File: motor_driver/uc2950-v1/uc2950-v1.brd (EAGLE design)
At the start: 165.6 x 63.7 mm, 76 parts, among them IC1 ATMEGA2560-16AU, IC2 ATMEGA2560-16AU, IC3 ATMEGA2560-16AU, IC4 ACS712, IC5 ACS712, IC6 ACS712, Y2 16MHz, Y3 16MHz, Y4 16MHz

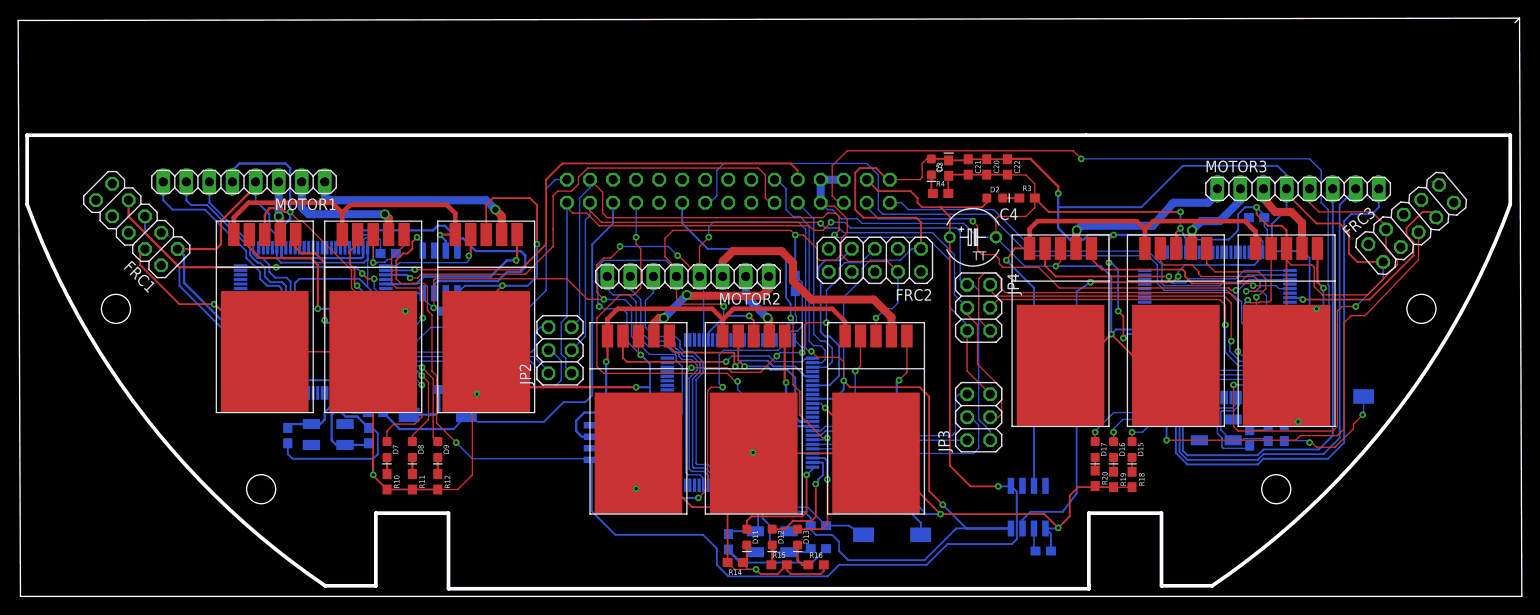
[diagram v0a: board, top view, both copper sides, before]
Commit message: added 12v, fixed previous issues
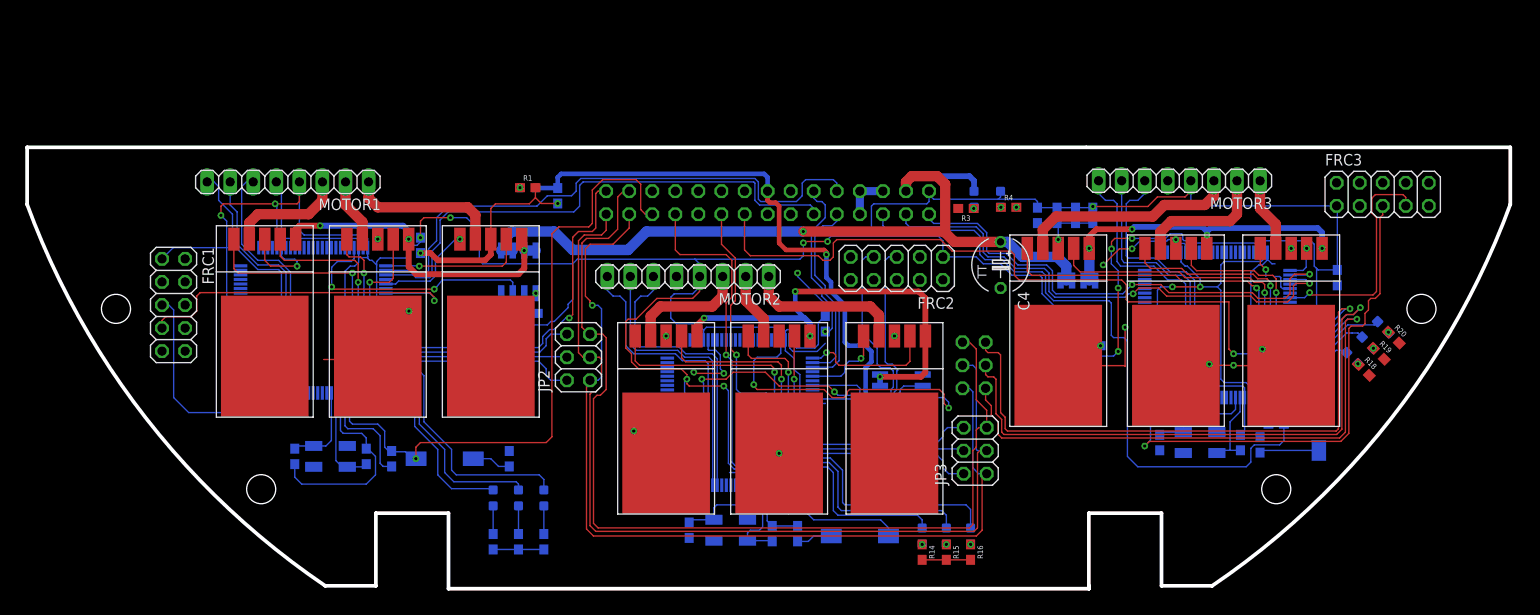
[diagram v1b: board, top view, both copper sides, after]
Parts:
- added C1: 10uF, SparkFun-Capacitors:0603-POLAR
- added D1: Yellow, SparkFun-LED:LED-0603
- added R1: 1k, SparkFun-Resistors:0603
- moved R20 36.4 mm to (150.7, 28.8), turned to 315 degrees
- moved D17 34.5 mm to (149.6, 30.0), flipped to the bottom, turned to 225 degrees
- moved R19 32.3 mm to (149.1, 27.1), turned to 315 degrees
- moved IC5 32.2 mm to (96.5, 22.9)
- moved C23 31.3 mm to (96.4, 19.1)
- moved D16 30.4 mm to (147.9, 28.3), flipped to the bottom, turned to 225 degrees
- moved R18 28.2 mm to (147.4, 25.3), turned to 315 degrees
- moved MIC6 28.2 mm to (90.4, 25.4)
- moved D15 26.3 mm to (146.2, 26.6), flipped to the bottom, turned to 225 degrees
- moved MIC7 25.4 mm to (134.1, 35.1)
- moved MIC9 25.1 mm to (108.5, 35.1)
- moved C24 23.3 mm to (117.6, 27.9)
- moved IC6 23.3 mm to (116.0, 32.8)
- moved MIC4 23.1 mm to (65.3, 25.4)
- moved R14 20.6 mm to (98.8, 5.21), turned to 270 degrees
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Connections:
- removed net N$11: C2.1, IC1.98
- removed net N$24: C3.1, IC3.98
- removed net N$26: C14.1, IC2.98
- new net 12V: C1.+, D1.A, IC5.1, IC5.2, JP1.16
- new net N$1: D1.C, R1.1
- net 18V: now also IC4.2, IC6.2; no longer IC5.1
- net 5V: now also C14.1, C2.1, C3.1, IC1.98, IC2.98, IC3.98
- net ACS1: now also IC4.4, MIC1.P$5, MIC2.P$5, MIC3.P$5; no longer MIC1.P$1, MIC2.P$1, MIC3.P$1
- net ACS2: now also IC5.4, MIC4.P$5, MIC5.P$5, MIC6.P$5; no longer MIC4.P$1, MIC5.P$1, MIC6.P$1
- net ACS3: now also IC6.4, MIC7.P$5, MIC8.P$5, MIC9.P$5; no longer MIC7.P$1, MIC8.P$1, MIC9.P$1
- net GND: now also C1.-, R1.2
- net M11: now also MIC3.P$2; no longer MIC3.P$4
- net M12: now also MIC6.P$2; no longer MIC6.P$4
- net M13: now also MIC7.P$2; no longer MIC7.P$4
- net M21: now also MIC2.P$2; no longer MIC2.P$4
- net M22: now also MIC5.P$2; no longer MIC5.P$4
- net M23: now also MIC8.P$2; no longer MIC8.P$4
- net M31: now also MIC1.P$2; no longer MIC1.P$4
- net M32: now also MIC4.P$2; no longer MIC4.P$4
- net M33: now also MIC9.P$2; no longer MIC9.P$4
- net MISO: now also JP2.1, JP3.1, JP4.1; no longer JP2.3, JP3.3, JP4.3
- net MISO1: now also JP2.2; no longer JP2.4
- net MISO2: now also JP3.2; no longer JP3.4
- net MISO3: now also JP4.2; no longer JP4.4
- net MOSI: now also JP2.3, JP3.3, JP4.3; no longer JP2.1, JP3.1, JP4.1
- net MOSI1: now also JP2.4; no longer JP2.2
- net MOSI2: now also JP3.4; no longer JP3.2
- net MOSI3: now also JP4.4; no longer JP4.2
- net S11: now also MIC3.P$4; no longer MIC3.P$2
- net S12: now also MIC6.P$4; no longer MIC6.P$2
- net S13: now also MIC7.P$4; no longer MIC7.P$2
- net S21: now also MIC3.P$1; no longer MIC3.P$5
- net S22: now also MIC6.P$1; no longer MIC6.P$5
- net S23: now also MIC7.P$1; no longer MIC7.P$5
- net S31: now also MIC2.P$4; no longer MIC2.P$2
- net S32: now also MIC5.P$4; no longer MIC5.P$2
- net S33: now also MIC8.P$4; no longer MIC8.P$2
- net S41: now also MIC2.P$1; no longer MIC2.P$5
- net S42: now also MIC5.P$1; no longer MIC5.P$5
- net S43: now also MIC8.P$1; no longer MIC8.P$5
- net S51: now also MIC1.P$4; no longer MIC1.P$2
- net S52: now also MIC4.P$4; no longer MIC4.P$2
- net S53: now also MIC9.P$4; no longer MIC9.P$2
- net S61: now also MIC1.P$1; no longer MIC1.P$5
- net S62: now also MIC4.P$1; no longer MIC4.P$5
- net S63: now also MIC9.P$1; no longer MIC9.P$5
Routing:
- net GND: track 710.4 -> 222.8 mm, vias 28 -> 25
- net 18V: track 161.9 -> 92.2 mm, vias 3 -> 1
- net 12V: track 0.00 -> 63.5 mm, vias 0 -> 1
- net MOSI3: track 40.2 -> 71.2 mm
- net 5V: track 478.6 -> 449.9 mm, vias 15 -> 11
- net MISO3: track 39.5 -> 67.4 mm
- net CLK: track 80.6 -> 108.2 mm, vias 1 -> 0
- net S13: track 30.5 -> 4.03 mm
- net H33: track 57.5 -> 31.4 mm
- net ACS3: track 61.9 -> 36.4 mm, vias 1 -> 4
- net H23: track 53.6 -> 30.0 mm
- net S63: track 14.5 -> 37.7 mm
- net CLK3: track 48.5 -> 71.0 mm
- net MISO: track 81.2 -> 102.5 mm
- net H13: track 51.2 -> 31.2 mm
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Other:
- board size 165.6 x 63.7 mm -> 163.3 x 48.6 mm

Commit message: header pin placement changed
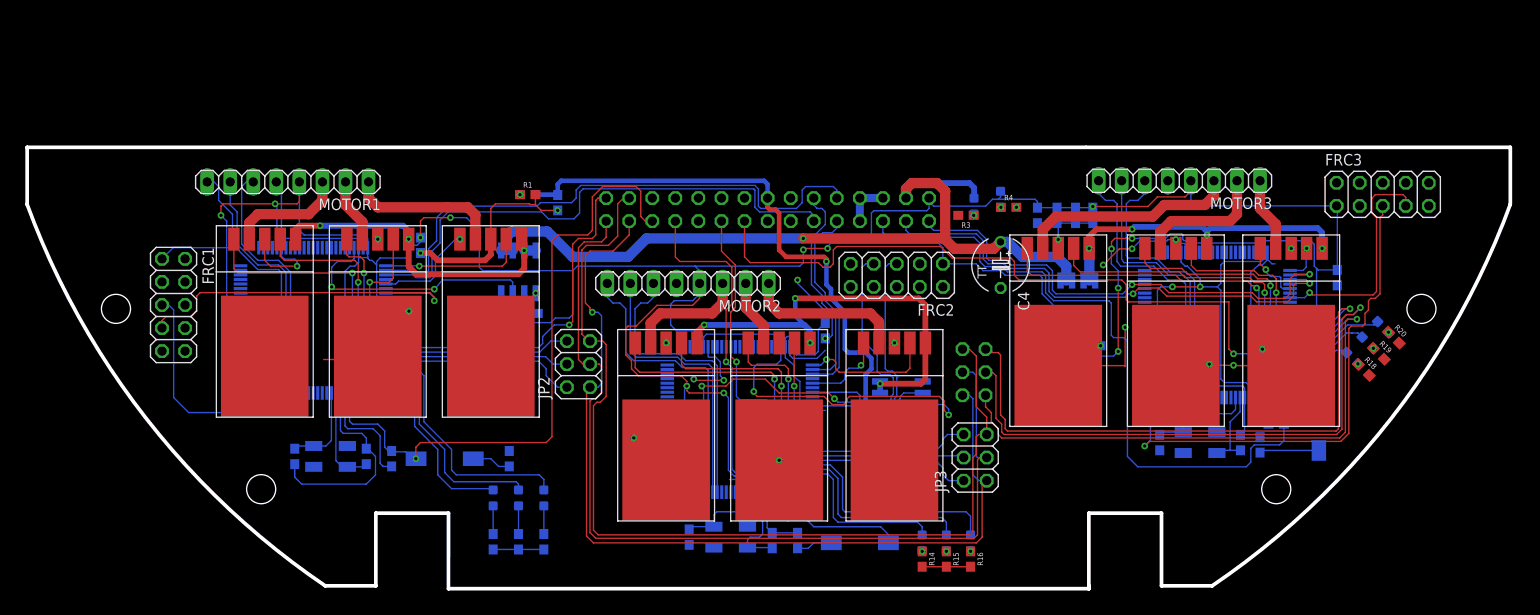
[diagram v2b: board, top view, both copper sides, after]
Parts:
- moved C1 0.76 mm to (58.7, 43.7)
- moved C14 0.76 mm to (88.1, 29.6)
- moved C16 0.76 mm to (73.2, 6.86)
- moved C23 0.76 mm to (96.4, 18.3)
- moved D1 0.76 mm to (55.4, 44.6)
- moved D11 0.76 mm to (98.8, 6.22)
- moved D12 0.76 mm to (101.5, 6.22)
- moved D13 0.76 mm to (104.1, 6.22)
- moved D2 0.76 mm to (104.5, 43.3)
- moved FRC2 0.76 mm to (96.0, 35.7)
- moved IC2 0.76 mm to (78.7, 19.8)
- moved IC5 0.76 mm to (96.5, 22.1)
- moved JP1 0.76 mm to (81.8, 48.0)
- moved JP2 0.76 mm to (61.0, 25.9)
- moved JP4 0.76 mm to (104.5, 25.0)
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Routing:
- net SS3: track 77.2 -> 76.4 mm
- net RST1: track 71.2 -> 70.4 mm
- net MISO3: track 67.4 -> 66.6 mm
- net CLK3: track 71.0 -> 70.3 mm
- net CLK1: track 21.2 -> 20.4 mm
- net MOSI3: track 71.2 -> 70.5 mm
- net 18V: track 92.2 -> 92.8 mm
- net S23: track 6.28 -> 6.87 mm
